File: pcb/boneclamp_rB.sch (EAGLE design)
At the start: 72 parts, among them IC1 24C, U1 AD8032ARZ-REEL7, U2 LT1964ES5-5TRMPBF, U4 TLV70245DBVT, U7 AD7682BCPZ, U8 TPS63700DRCT, U9 ADA4841-2YRZ

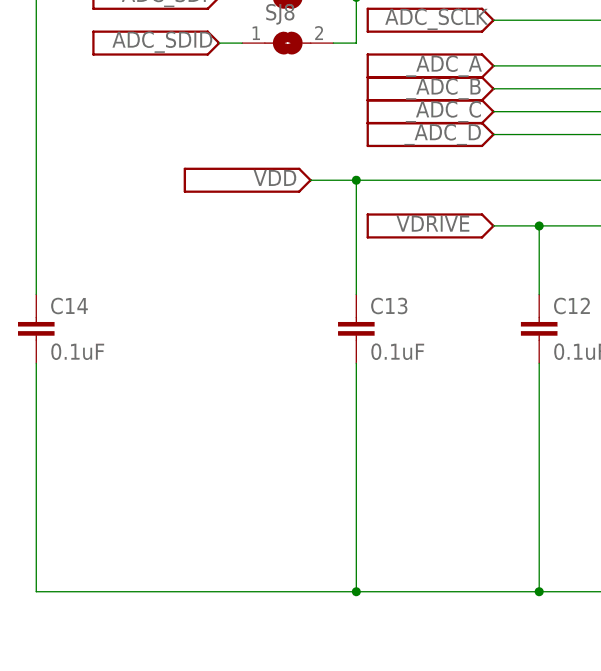
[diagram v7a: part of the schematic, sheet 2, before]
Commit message: Added Ground and power plane to pcb. Power plane will need to be split into primarly VDD and then a bit at the front of the board for VSS. VDD and VSS planes should not overlap in the Z direction.
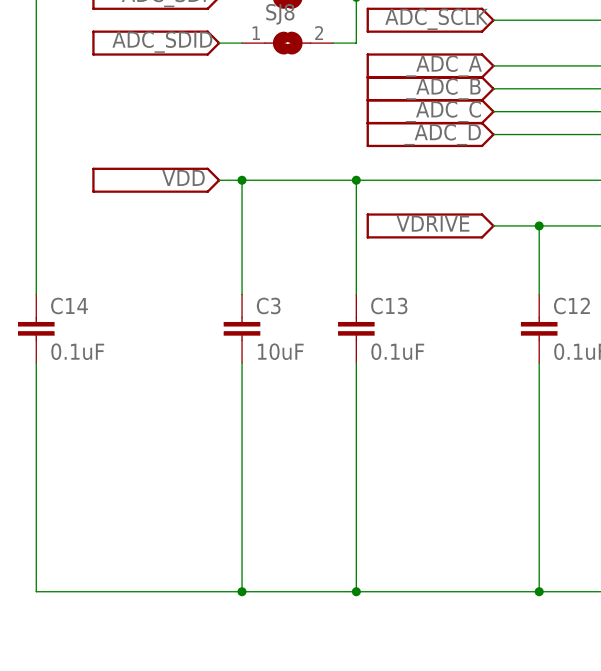
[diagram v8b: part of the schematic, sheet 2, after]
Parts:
- added C3: 10uF, rcl:C-EUC0805
- C23, C24, C26, C27, C29, C30, C31, C32, C33, C34, C35, C5, C6, C7, C8, C9: device rcl:C-EUC0805 -> rcl:C-EUC0603
- R12, R13, R5: device resistor:R-US_R0805 -> rcl:R-US_R0603
- renumbered U$27 to D1, U$28 to L1
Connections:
- net AGND: now also C3.2
- net VDD: now also C3.1
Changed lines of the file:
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@@
 <part name="U8" library="ti-extended" deviceset="TPS63700DRCT" device=""/>
 <part name="U$18" library="boneclamp" deviceset="V_SIG" device=""/>
-<part name="C23" library="rcl" deviceset="C-EU" device="C0805" value="10uF"/>
-<part name="R5" library="resistor" deviceset="R-US_" device="R0805" value="100k"/>
-<part name="C24" library="rcl" deviceset="C-EU" device="C0805" value="22nF"/>
-<part name="C26" library="rcl" deviceset="C-EU" device="C0805" value="0.1uF"/>
+<part name="C23" library="rcl" deviceset="C-EU" device="C0603" value="10uF"/>
+<part name="R5" library="rcl" deviceset="R-US_" device="R0603" value="100k"/>
+<part name="C24" library="rcl" deviceset="C-EU" device="C0603" value="22nF"/>
+<part name="C26" library="rcl" deviceset="C-EU" device="C0603" value="0.1uF"/>
 <part name="SUPPLY21" library="supply2" deviceset="AGND" device=""/>
-<part name="C27" library="rcl" deviceset="C-EU" device="C0805" value="4.7nF"/>
+<part name="C27" library="rcl" deviceset="C-EU" device="C0603" value="4.7nF"/>
 <part name="SUPPLY24" library="supply2" deviceset="AGND" device=""/>
-<part name="U$27" library="boneclamp" deviceset="SCHOTTKY-DIODE-2" device="" value=""/>
-<part name="U$28" library="boneclamp" deviceset="L-US" device="" value="4.7uH"/>
-<part name="C29" library="rcl" deviceset="C-EU" device="C0805" value="10nF"/>
-<part name="C30" library="rcl" deviceset="C-EU" device="C0805" value="4.7uF"/>
-<part name="C31" library="rcl" deviceset="C-EU" device="C0805" value="4.7uF"/>
-<part name="C32" library="rcl" deviceset="C-EU" device="C0805" value="4.7uF"/>
-<part name="C33" library="rcl" deviceset="C-EU" device="C0805" value="4.7uF"/>
-<part name="R12" library="resistor" deviceset="R-US_" device="R0805" value="750"/>
-<part name="R13" library="resistor" deviceset="R-US_" device="R0805" value="150k"/>
-<part name="C34" library="rcl" deviceset="C-EU" device="C0805" value="0.22uF"/>
+<part name="D1" library="boneclamp" deviceset="SCHOTTKY-DIODE-2" device="" value=""/>
+<part name="L1" library="boneclamp" deviceset="L-US" device="" value="4.7uH"/>
+<part name="C29" library="rcl" deviceset="C-EU" device="C0603" value="10nF"/>
+<part name="C30" library="rcl" deviceset="C-EU" device="C0603" value="4.7uF"/>
+<part name="C31" library="rcl" deviceset="C-EU" device="C0603" value="4.7uF"/>
+<part name="C32" library="rcl" deviceset="C-EU" device="C0603" value="4.7uF"/>
+<part name="C33" library="rcl" deviceset="C-EU" device="C0603" value="4.7uF"/>
+<part name="R12" library="rcl" deviceset="R-US_" device="R0603" value="750"/>
+<part name="R13" library="rcl" deviceset="R-US_" device="R0603" value="150k"/>
+<part name="C34" library="rcl" deviceset="C-EU" device="C0603" value="0.22uF"/>
 <part name="SUPPLY3" library="supply2" deviceset="AGND" device=""/>
 <part name="U$29" library="boneclamp" deviceset="V_SIG" device=""/>
-<part name="C35" library="rcl" deviceset="C-EU" device="C0805" value="10pF"/>
+<part name="C35" library="rcl" deviceset="C-EU" device="C0603" value="10pF"/>
 <part name="U2" library="linear-extended-01" deviceset="LT1964ES5-5TRMPBF" device=""/>
 <part name="U$19" library="boneclamp" deviceset="V_SIG" device=""/>
 <part name="SUPPLY9" library="supply2" deviceset="AGND" device=""/>
-<part name="C5" library="rcl" deviceset="C-EU" device="C0805" value="1uF"/>
-<part name="C6" library="rcl" deviceset="C-EU" device="C0805" value="10nF"/>
-<part name="C7" library="rcl" deviceset="C-EU" device="C0805" value="10uF"/>
+<part name="C5" library="rcl" deviceset="C-EU" device="C0603" value="1uF"/>
+<part name="C6" library="rcl" deviceset="C-EU" device="C0603" value="10nF"/>
+<part name="C7" library="rcl" deviceset="C-EU" device="C0603" value="10uF"/>
 <part name="U$20" library="boneclamp" deviceset="V_SIG" device=""/>
 <part name="TP5" library="testpad" deviceset="TP" device="B1,27"/>
 <part name="TP6" library="testpad" deviceset="TP" device="B1,27"/>
 <part name="U4" library="ti-extended" deviceset="TLV70025DDCR" device="" value="TLV70245DBVT"/>
-<part name="C8" library="rcl" deviceset="C-EU" device="C0805" value="1uF"/>
-<part name="C9" library="rcl" deviceset="C-EU" device="C0805" value="1uF"/>
+<part name="C8" library="rcl" deviceset="C-EU" device="C0603" value="1uF"/>
+<part name="C9" library="rcl" deviceset="C-EU" device="C0603" value="1uF"/>
 <part name="SUPPLY10" library="supply2" deviceset="AGND" device=""/>
 <part name="U$21" library="boneclamp" deviceset="V_SIG" device=""/>
@@
 <part name="SUPPLY4" library="supply2" deviceset="AGND" device=""/>
 <part name="TP7" library="testpad" deviceset="TP" device="B1,27"/>
+<part name="C3" library="rcl" deviceset="C-EU" device="C0805" value="10uF"/>
 </parts>
 <sheets>
@@
 <instance part="U$13" gate="G$1" x="33.02" y="7.62"/>
 <instance part="U$14" gate="G$1" x="-33.02" y="-12.7" rot="MR0"/>
-<instance part="U$15" gate="G$1" x="-53.34" y="-7.62" rot="MR0"/>
+<instance part="U$15" gate="G$1" x="-63.5" y="-7.62" rot="MR0"/>
 <instance part="U$32" gate="G$1" x="-63.5" y="12.7" rot="MR0"/>
 <instance part="U$43" gate="G$1" x="-33.02" y="10.16" rot="MR0"/>
@@
 <instance part="C2" gate="G$1" x="81.28" y="25.4"/>
 <instance part="SUPPLY4" gate="G$1" x="81.28" y="15.24"/>
+<instance part="C3" gate="G$1" x="-60.96" y="-22.86"/>
 </instances>
 <busses>
@@
 <pinref part="C14" gate="G$1" pin="2"/>
 <wire x1="-83.82" y1="-27.94" x2="-83.82" y2="-53.34" width="0.1524" layer="91"/>
-<wire x1="-83.82" y1="-53.34" x2="-48.26" y2="-53.34" width="0.1524" layer="91"/>
+<wire x1="-83.82" y1="-53.34" x2="-60.96" y2="-53.34" width="0.1524" layer="91"/>
 <junction x="-48.26" y="-53.34"/>
 <pinref part="U1" gate="A" pin="-VS"/>
+<wire x1="-60.96" y1="-53.34" x2="-48.26" y2="-53.34" width="0.1524" layer="91"/>
 <wire x1="116.84" y1="-53.34" x2="116.84" y2="-5.08" width="0.1524" layer="91"/>
 <pinref part="R16" gate="G$1" pin="2"/>
@@
 <wire x1="104.14" y1="-27.94" x2="104.14" y2="-53.34" width="0.1524" layer="91"/>
 <junction x="104.14" y="-53.34"/>
+<pinref part="C3" gate="G$1" pin="2"/>
+<wire x1="-60.96" y1="-27.94" x2="-60.96" y2="-53.34" width="0.1524" layer="91"/>
+<junction x="-60.96" y="-53.34"/>
 </segment>
 <segment>
@@
 <wire x1="-20.32" y1="-10.16" x2="-20.32" y2="-7.62" width="0.1524" layer="91"/>
 <junction x="-20.32" y="-7.62"/>
-<wire x1="-48.26" y1="-7.62" x2="-53.34" y2="-7.62" width="0.1524" layer="91"/>
+<wire x1="-48.26" y1="-7.62" x2="-60.96" y2="-7.62" width="0.1524" layer="91"/>
 <junction x="-48.26" y="-7.62"/>
-<label x="-59.69" y="-8.255" size="1.778" layer="95"/>
+<label x="-69.85" y="-8.255" size="1.778" layer="95"/>
+<pinref part="C3" gate="G$1" pin="1"/>
+<wire x1="-60.96" y1="-7.62" x2="-63.5" y2="-7.62" width="0.1524" layer="91"/>
+<wire x1="-60.96" y1="-20.32" x2="-60.96" y2="-7.62" width="0.1524" layer="91"/>
+<junction x="-60.96" y="-7.62"/>
 </segment>
 </net>
@@
 <instance part="C27" gate="G$1" x="25.4" y="48.26"/>
 <instance part="SUPPLY24" gate="G$1" x="0" y="27.94"/>
-<instance part="U$27" gate="G$1" x="43.18" y="60.96" rot="R90"/>
-<instance part="U$28" gate="G$1" x="35.56" y="50.8"/>
+<instance part="D1" gate="G$1" x="43.18" y="60.96" rot="R90"/>
+<instance part="L1" gate="G$1" x="35.56" y="50.8"/>
 <instance part="C29" gate="G$1" x="60.96" y="48.26"/>
 <instance part="C30" gate="G$1" x="73.66" y="48.26"/>
@@
 <wire x1="25.4" y1="30.48" x2="35.56" y2="30.48" width="0.1524" layer="91"/>
 <junction x="25.4" y="30.48"/>
-<pinref part="U$28" gate="G$1" pin="2"/>
+<pinref part="L1" gate="G$1" pin="2"/>
 <wire x1="35.56" y1="30.48" x2="35.56" y2="43.18" width="0.1524" layer="91"/>
 <wire x1="35.56" y1="30.48" x2="60.96" y2="30.48" width="0.1524" layer="91"/>
@@
 <pinref part="U8" gate="A" pin="OUT"/>
 <wire x1="48.26" y1="66.04" x2="17.78" y2="66.04" width="0.1524" layer="91"/>
-<pinref part="U$27" gate="G$1" pin="C"/>
+<pinref part="D1" gate="G$1" pin="C"/>
 <wire x1="48.26" y1="60.96" x2="60.96" y2="60.96" width="0.1524" layer="91"/>
 <junction x="48.26" y="60.96"/>
@@
 <net name="N$27" class="0">
 <segment>
-<pinref part="U$27" gate="G$1" pin="A"/>
+<pinref part="D1" gate="G$1" pin="A"/>
 <pinref part="U8" gate="A" pin="SW"/>
 <wire x1="17.78" y1="60.96" x2="35.56" y2="60.96" width="0.1524" layer="91"/>
-<pinref part="U$28" gate="G$1" pin="1"/>
+<pinref part="L1" gate="G$1" pin="1"/>
 <wire x1="35.56" y1="60.96" x2="40.64" y2="60.96" width="0.1524" layer="91"/>
 <wire x1="35.56" y1="58.42" x2="35.56" y2="60.96" width="0.1524" layer="91"/>
